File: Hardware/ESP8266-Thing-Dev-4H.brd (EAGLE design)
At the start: 55.4 x 25.9 mm, 70 parts, among them J1 U.FL, Q1 MMBT2222A, Q2 MMBT2222A, U1 AP2112K-3.3V, U2 ESP8266, U3 AT25SF041-SOIC8, U4 FTS31XS-U, Y1 26MHz

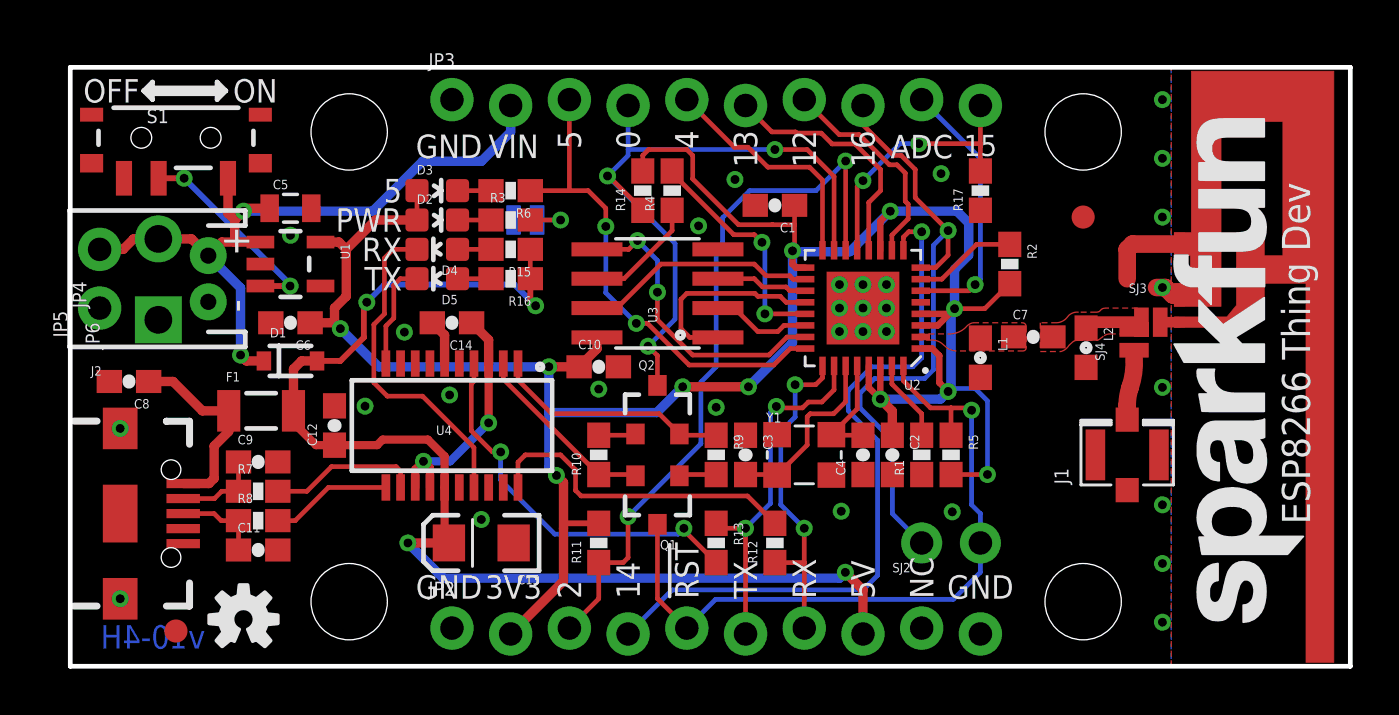
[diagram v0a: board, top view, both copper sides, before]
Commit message: Updating libraries, increasing width of 4H logo lines.
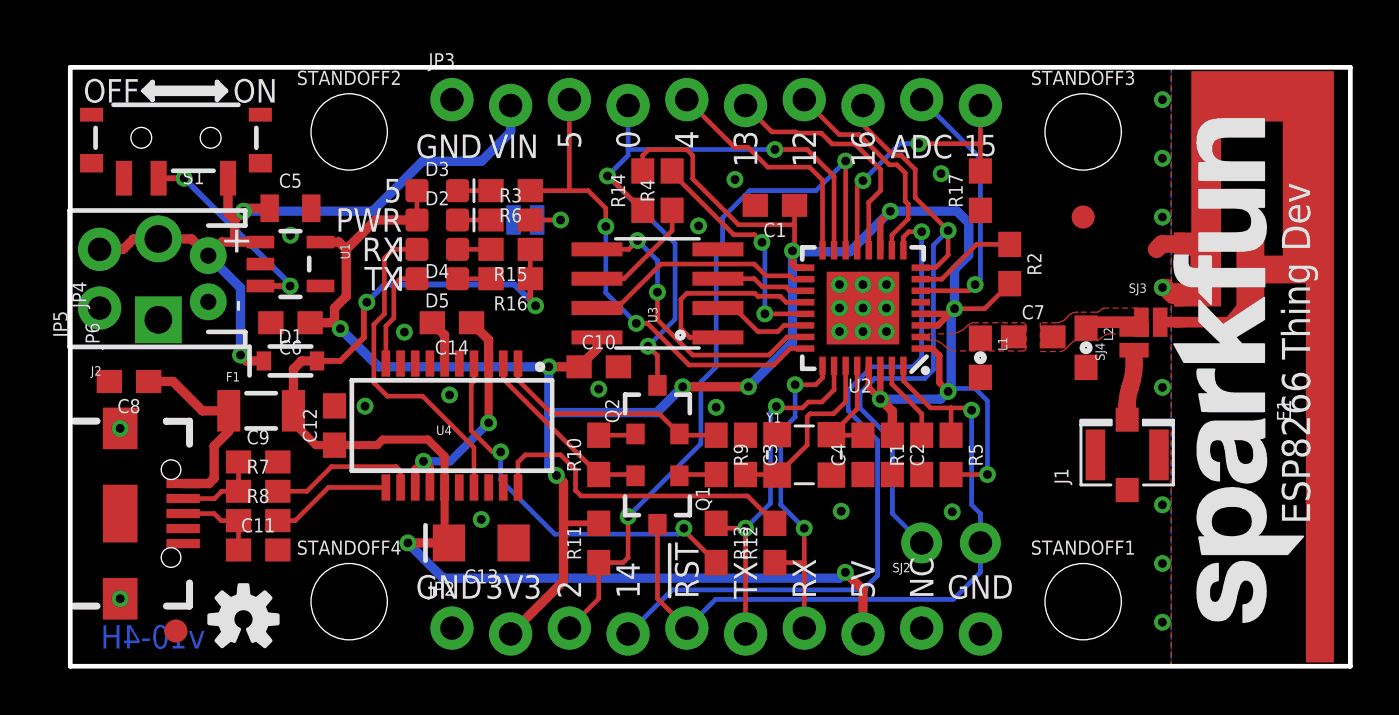
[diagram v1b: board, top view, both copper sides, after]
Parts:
- C1, C10, C11, C12, C14, C2, C3, C4, C6, C8, C9: device SparkFun-Capacitors:0603-CAP -> SparkFun-Capacitors:0603
- C7: value 5.6pF -> 5.6PF; device SparkFun-Capacitors:0603-CAP -> SparkFun-Capacitors:0603
- D1: value BAT20J -> 1A/23V/620mV
- E1: value ANTENNATRACE -> (none)
- Q1, Q2: value MMBT2222A -> 600mA/40V
- R1, R3, R4, R6, R7, R8: device SparkFun-Resistors:0603-RES -> SparkFun-Resistors:0603
- R10, R11, R14, R17, R2, R5, R9: value 10K -> 10k; device SparkFun-Resistors:0603-RES -> SparkFun-Resistors:0603
- R12, R13, R15, R16: value 1K -> 1k; device SparkFun-Resistors:0603-RES -> SparkFun-Resistors:0603
- S1: device SparkFun-Electromechanical:SWITCH-SPST-SMD-A -> SparkFun-Switches:SWITCH_SPST_SMD_A
- STANDOFF1, STANDOFF2, STANDOFF3, STANDOFF4: device SparkFun-Electromechanical:STAND-OFF -> SparkFun-Hardware:STAND-OFF
- U2: device esp8266-development-board:QFN32 -> SparkFun-RF:QFN32-5X5MM
- turned D2 to 0 degrees
- turned D3 to 0 degrees
- turned D4 to 180 degrees
- turned D5 to 180 degrees
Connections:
- net GND: now also C13.-; no longer C13.C
- net USBVCC: now also C13.+; no longer C13.A
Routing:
- net GND: track 6.74 -> 3.94 mm
